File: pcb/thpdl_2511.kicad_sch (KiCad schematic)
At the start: 35 parts

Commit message: update drawing sheet table on schematic too
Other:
- company: https://github.com/sthivaios -> Stratos Thivaios (c) 2025 - https://github.com/sthivaios
- title: ESP32-Powered BME680 Environmental Sensor IoT Device -> THPDL-2511
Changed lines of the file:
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@@
 	(paper "A4")
 	(title_block
-		(title "ESP32-Powered BME680 Environmental Sensor IoT Device")
-		(date "2025-11-23")
+		(title "THPDL-2511")
+		(date "2025-12-01")
 		(rev "1.0")
-		(company "https://github.com/sthivaios")
+		(company "Stratos Thivaios (c) 2025 - https://github.com/sthivaios")
 	)
 	(rectangle

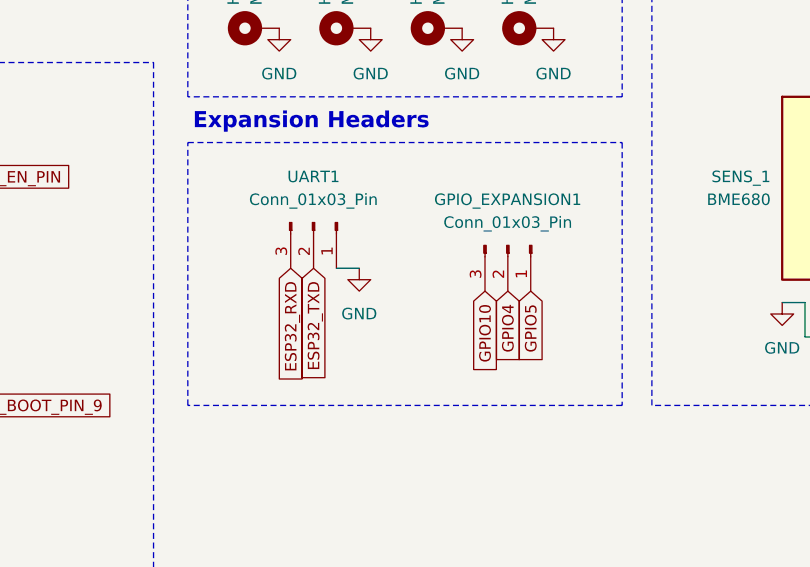
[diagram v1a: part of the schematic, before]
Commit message: add i2c header
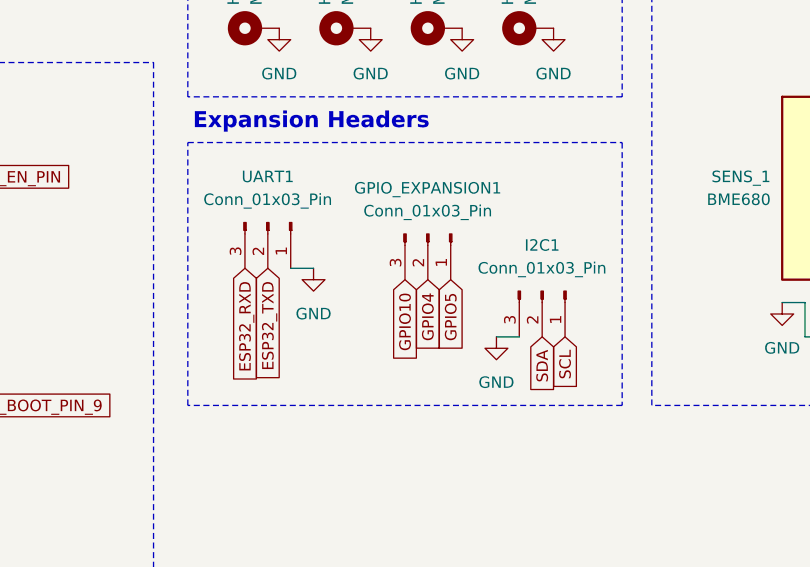
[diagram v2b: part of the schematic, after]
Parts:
- added I2C1: Conn_01x03_Pin, Connector_PinHeader_2.54mm:PinHeader_1x03_P2.54mm_Vertical, symbol Connector:Conn_01x03_Pin
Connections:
- net GND: now also I2C1.3 (Pin_3)
- net SCL: now also I2C1.1 (Pin_1)
- net SDA: now also I2C1.2 (Pin_2)
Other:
- moved on the sheet: GPIO_EXPANSION1, UART1
